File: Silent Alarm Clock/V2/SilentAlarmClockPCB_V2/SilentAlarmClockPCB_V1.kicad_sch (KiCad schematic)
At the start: 28 parts, among them J1 USB_C_Receptacle_USB2.0_16P, J2 Barrel_Jack, J3 B2B-PH-K-S, SW3 RESET, SW4 BOOT, U1 ESD7104MUTAG, U2 ESP32-S3-MINI-1-N8, U3 BQ24040DSQR, U4 TLV75801PDRV

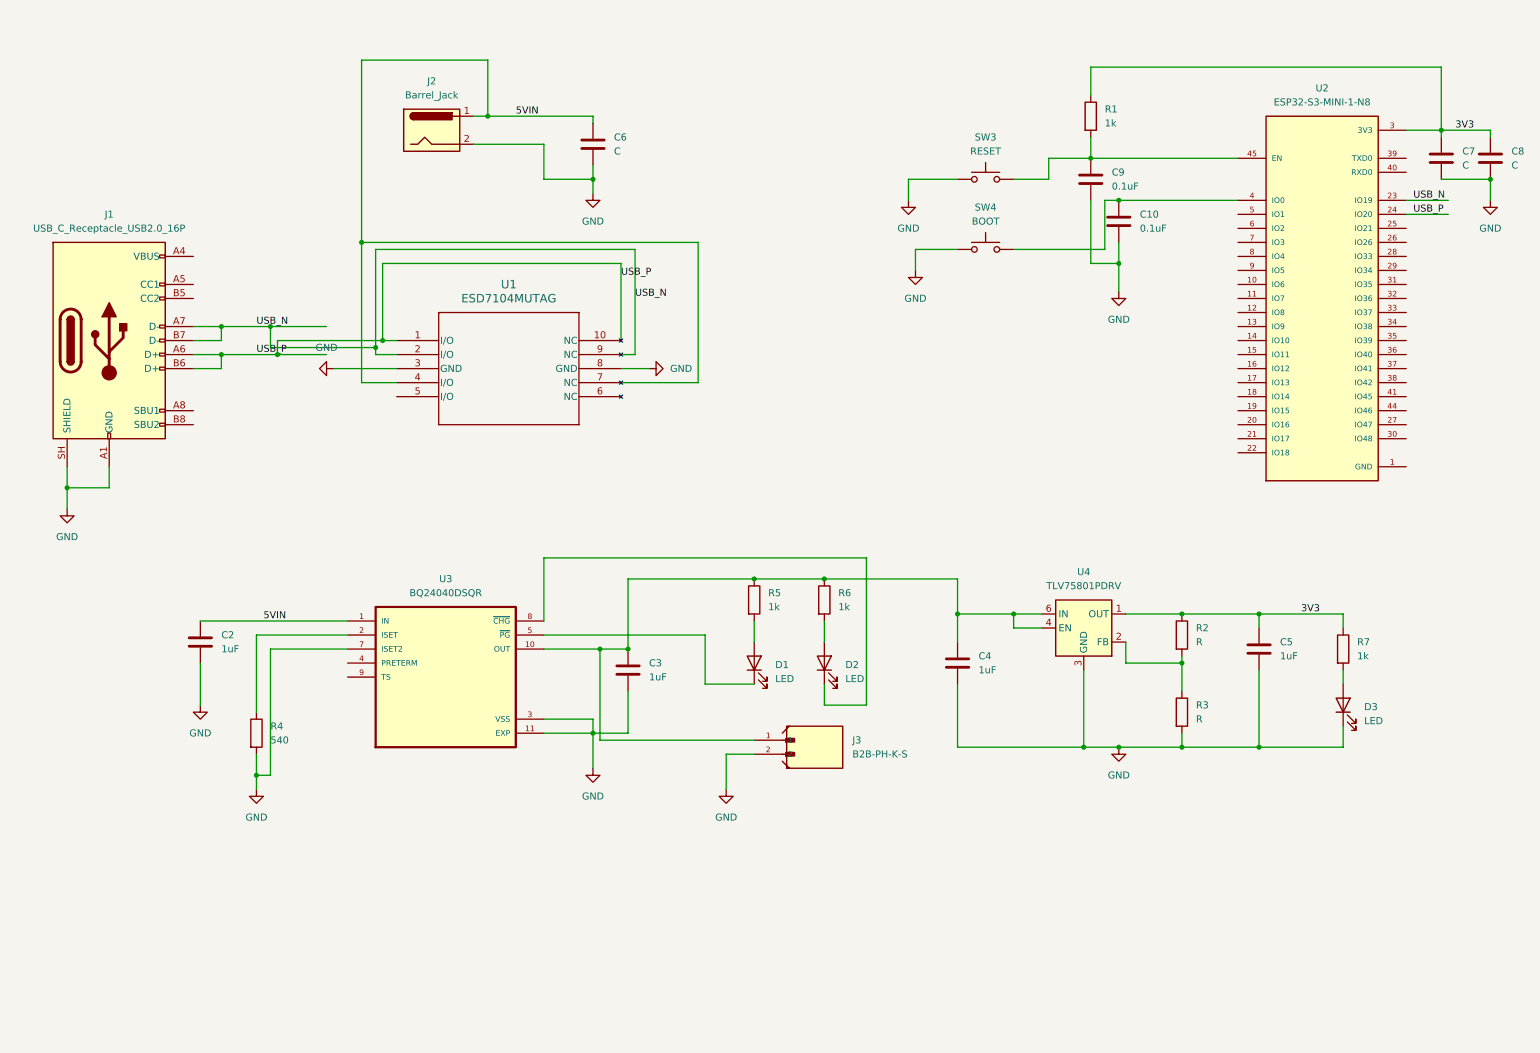
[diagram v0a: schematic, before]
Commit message: Beginning of sparkfun battery babysitter implementation
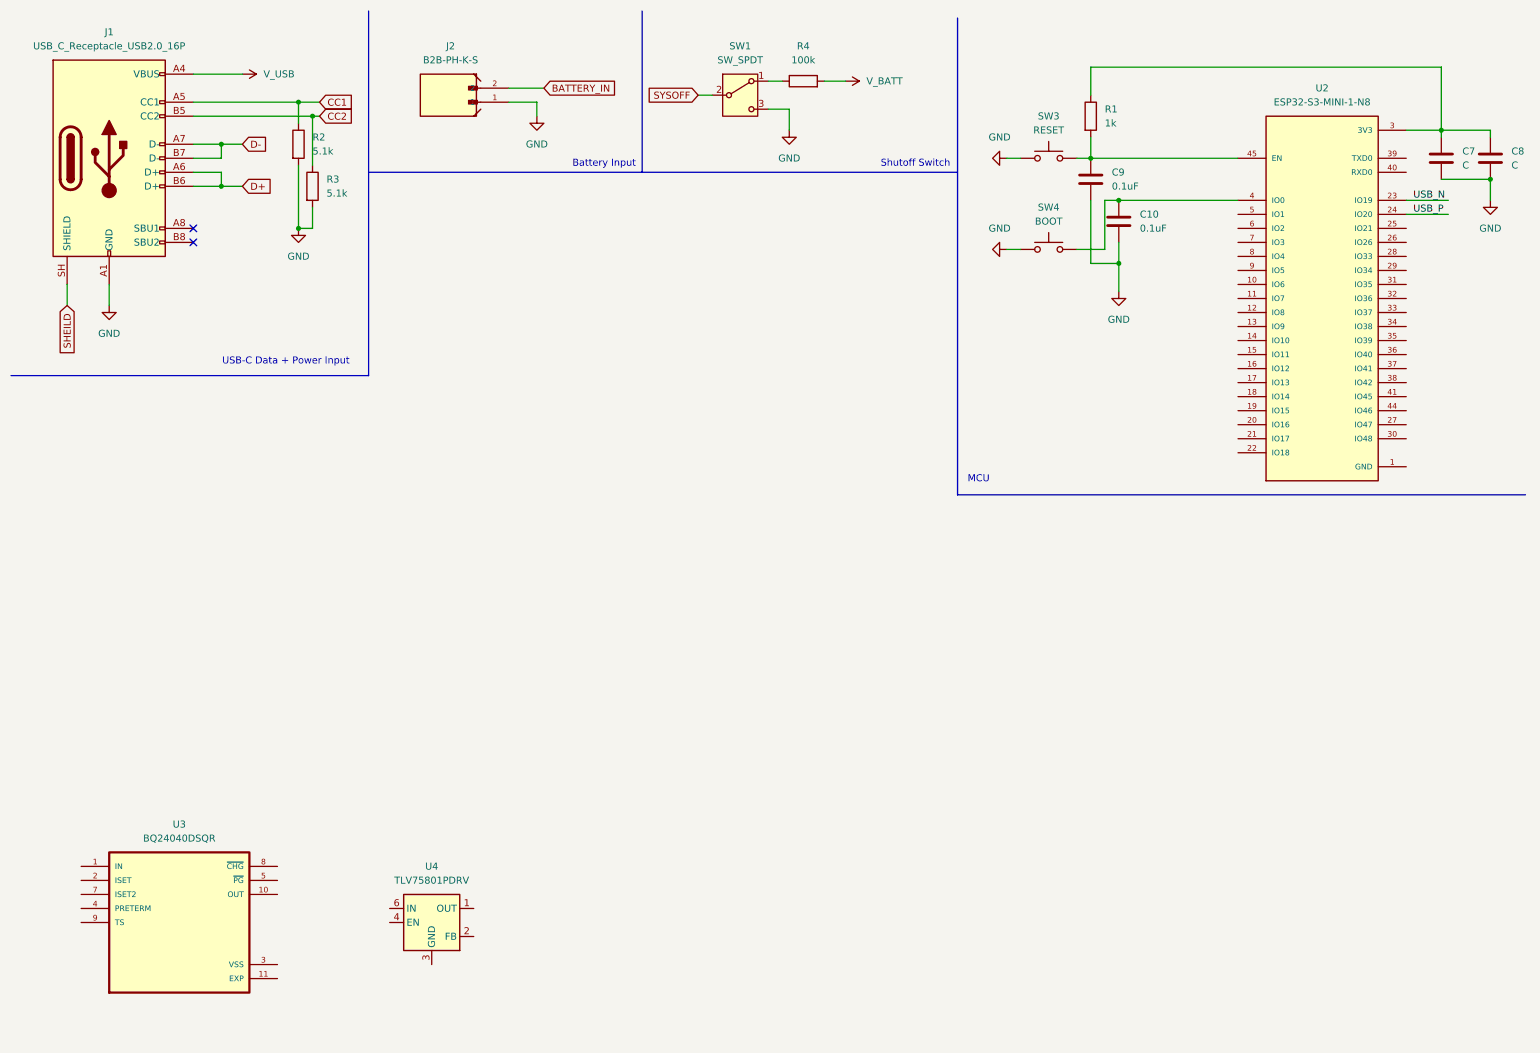
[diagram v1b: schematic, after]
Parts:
- removed C2, C3, C4, C5: 1uF, Capacitor_SMD:C_0603_1608Metric, symbol Device:C
- removed C6: C, Capacitor_SMD:C_0603_1608Metric, symbol Device:C
- removed D1, D2, D3: LED, LED_SMD:LED_0603_1608Metric, symbol Device:LED
- removed J2: Barrel_Jack, Connector_BarrelJack:BarrelJack_CLIFF_FC681465S_SMT_Horizontal, symbol Connector:Barrel_Jack
- removed J3: B2B-PH-K-S, B2B_PH_K_S:JST_B2B-PH-K-S, symbol B2B-PH-K-S:B2B-PH-K-S
- removed R5, R6, R7: 1k, Resistor_SMD:R_0603_1608Metric, symbol Device:R
- removed U1: ESD7104MUTAG, UDFN10_ONS, symbol ESD7104MUTAG:ESD7104MUTAG
- added J2: B2B-PH-K-S, B2B-PH-K-S:JST_B2B-PH-K-S, symbol B2B-PH-K-S:B2B-PH-K-S
- added SW1: SW_SPDT, symbol Switch:SW_SPDT
- R2, R3: value R -> 5.1k
- R4: value 540 -> 100k
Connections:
- net GND: now also R2.2, J2.1, SW1.3 (C); no longer J1.SH (SHIELD), R4.2, U3.11 (EXP), U3.3 (VSS), U3.7 (ISET2), U4.3 (GND), U4.7 (GND)
- net USB_N: no longer J1.A7 (D-), J1.B7 (D-)
- net USB_P: no longer J1.A6 (D+), J1.B6 (D+)
- net at U3.2 (ISET): no longer R4.1
- net V_USB: now reaches J1.A4 (VBUS), J1.A9 (VBUS), J1.B4 (VBUS), J1.B9 (VBUS)
- net CC1: now reaches J1.A5 (CC1)
- net CC1: now also R2.1
- net CC2: now reaches J1.B5 (CC2)
- net CC2: now also R3.1
- net 3V3: no longer names the net of C7.1, C8.1, R1.1, U2.3 (3V3)
- net 3V3: no longer R2.1, U4.1 (OUT)
- net 5VIN: no longer names the net of U3.1 (IN)
- new net: R4.1, SW1.1 (A)
- new net: U4.3 (GND), U4.7 (GND)
- new net BATTERY_IN: J2.2
- new net D+: J1.A6 (D+), J1.B6 (D+)
- new net D-: J1.A7 (D-), J1.B7 (D-)
- new net SHEILD: J1.SH (SHIELD)
- new net SYSOFF: SW1.2 (B)
- new net V_BATT: R4.2
- now unconnected: U3.10 (OUT), U4.2 (FB), U4.4 (EN), U4.6 (IN)
- no-connect marks 0 -> 2
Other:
- note added: "Battery Input"
- note added: "MCU"
- note added: "Shutoff Switch"
- note added: "USB-C Data + Power Input"
- moved on the sheet: J1, SW3, SW4, U3, U4

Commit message: V2 power schematic finished
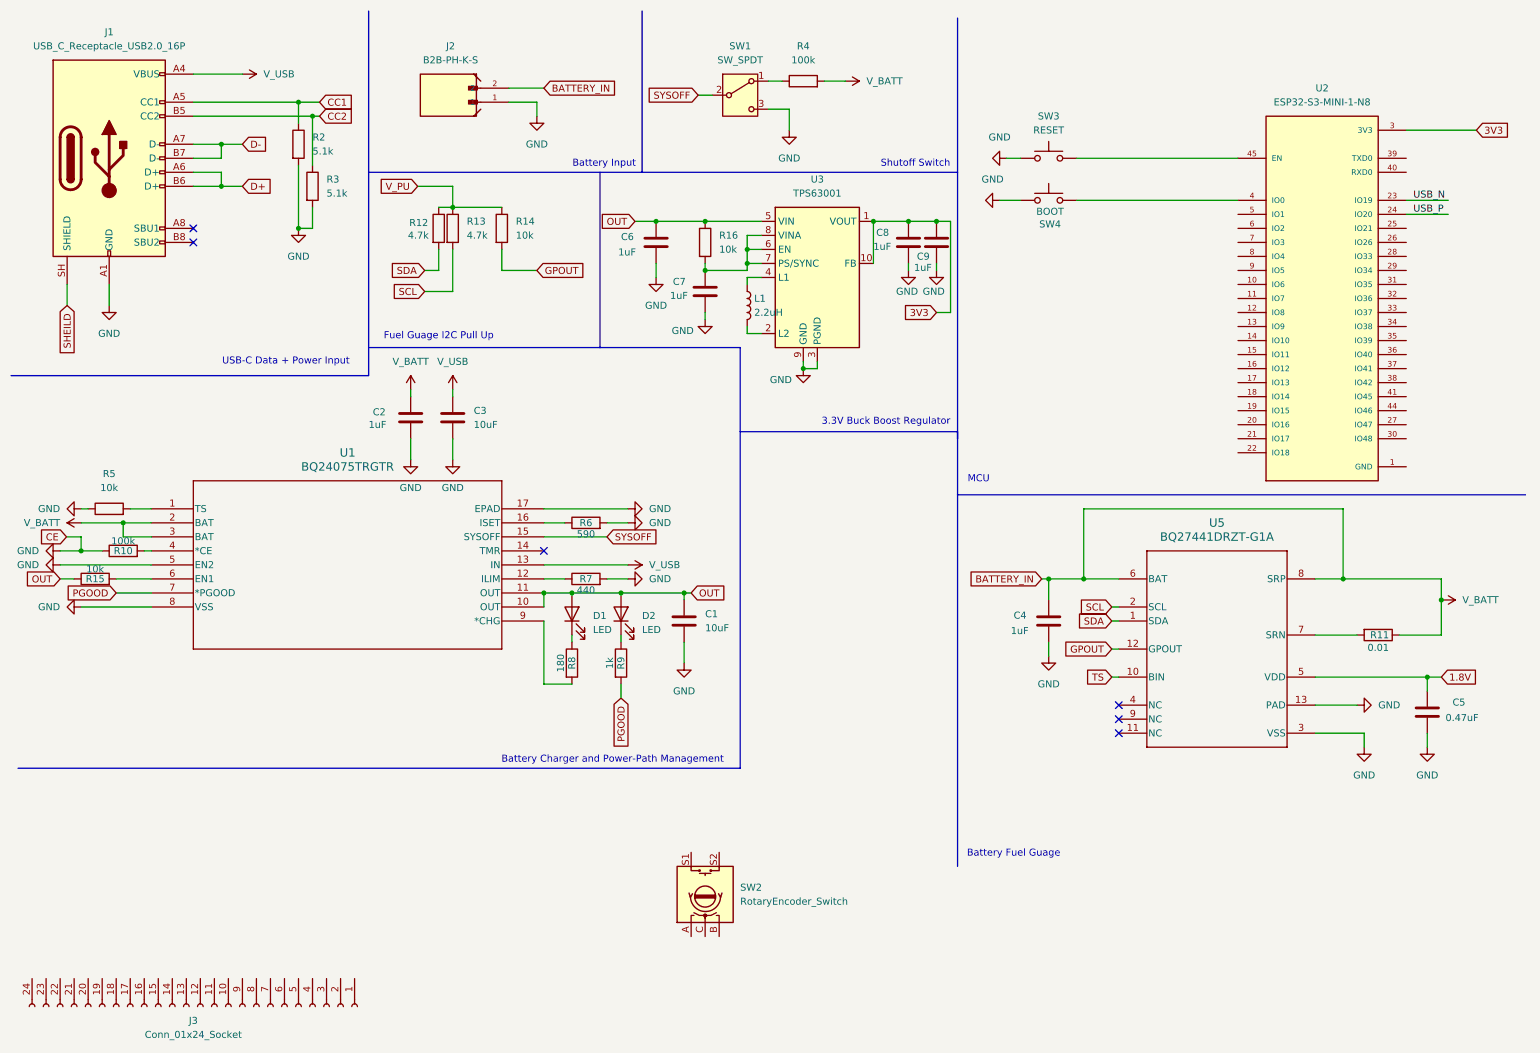
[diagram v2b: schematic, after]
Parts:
- removed C10: 0.1uF, Capacitor_SMD:C_0603_1608Metric, symbol Device:C
- removed R1: 1k, Resistor_SMD:R_0603_1608Metric, symbol Device:R
- removed U3: BQ24040DSQR, BQ24040DSQR:SON40P200X200X80-11N, symbol BQ24040DSQR:BQ24040DSQR
- removed U4: TLV75801PDRV, Package_SON:WSON-6-1EP_2x2mm_P0.65mm_EP1x1.6mm, symbol Regulator_Linear:TLV75801PDRV
- added C1, C3: 10uF, Capacitor_SMD:C_0603_1608Metric, symbol Device:C
- added C2, C4, C6: 1uF, Capacitor_SMD:C_0603_1608Metric, symbol Device:C
- added C5: 0.47uF, Capacitor_SMD:C_0603_1608Metric, symbol Device:C
- added D1, D2: LED, symbol Device:LED
- added J3: Conn_01x24_Socket, Connector_FFC-FPC:Hirose_FH12-24S-0.5SH_1x24-1MP_P0.50mm_Horizontal, symbol Connector:Conn_01x24_Socket
- added L1: 2.2uH, Inductor_SMD:L_1008_2520Metric, symbol Device:L
- added R10: 100k, Resistor_SMD:R_0603_1608Metric, symbol Device:R
- added R11: 0.01, Resistor_SMD:R_0603_1608Metric, symbol Device:R
- added R12, R13: 4.7k, Resistor_SMD:R_0603_1608Metric, symbol Device:R
- added R14, R15, R16, R5: 10k, Resistor_SMD:R_0603_1608Metric, symbol Device:R
- added R6: 590, Resistor_SMD:R_0603_1608Metric, symbol Device:R
- added R7: 440, Resistor_SMD:R_0603_1608Metric, symbol Device:R
- added R8: 180, Resistor_SMD:R_0603_1608Metric, symbol Device:R
- added R9: 1k, Resistor_SMD:R_0603_1608Metric, symbol Device:R
- added SW2: RotaryEncoder_Switch, symbol Device:RotaryEncoder_Switch
- added U1: BQ24075TRGTR, RGT16_1P7X1P7, symbol 2026-08-07_15-47-46:BQ24075TRGTR
- added U3: TPS63001, Package_SON:Texas_DRC0010J_ThermalVias, symbol Regulator_Switching:TPS63001
- added U5: BQ27441DRZT-G1A, Copy of DRZ0012A, symbol BQ27441-G1A:BQ27441DRZT-G1A
- C7, C8: value C -> 1uF
- C9: value 0.1uF -> 1uF
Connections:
- net BATTERY_IN is gone; now on net V_BATT: J2.2
- net GND: now also C7.1, C8.1, C9.1, C1.2, C2.2, C3.2, C4.1, C5.1, C6.1, R10.1, R5.1, R6.2, R7.2, U1.17 (EPAD), U1.5 (EN2), U1.8 (VSS), U3.11 (PGND), U3.3 (PGND), U3.9 (GND), U5.13 (PAD), U5.3 (VSS); no longer C7.2, C8.2, C9.2
- net SYSOFF: now also U1.15 (SYSOFF)
- net V_BATT: now also C2.1, C4.2, R11.1, U1.2 (BAT), U1.3 (BAT), U5.6 (BAT), U5.8 (SRP)
- net V_USB: now also C3.1, U1.13 (IN)
- net at SW3.2, U2.45 (EN): no longer C9.1
- new net: R11.2, U5.7 (SRN)
- new net: D1.1 (K), R8.1
- new net: R8.2, U1.9 (*CHG)
- new net: R5.2, U1.1 (TS)
- new net: D2.1 (K), R9.1
- new net: L1.1, U3.4 (L1)
- new net: L1.2, U3.2 (L2)
- new net: C7.2, R16.2, U3.6 (EN), U3.7 (PS/SYNC), U3.8 (VINA)
- new net: R10.2, U1.4 (*CE)
- new net: R15.2, U1.6 (EN1)
- new net: R7.1, U1.12 (ILIM)
- new net: R6.1, U1.16 (ISET)
- new net 1.8V: C5.2, U5.5 (VDD)
- new net 3V3: C8.2, C9.2, U2.3 (3V3), U3.1 (VOUT), U3.10 (FB)
- new net GPOUT: R14.2, U5.12 (GPOUT)
- new net OUT: C1.1, C6.2, D1.2 (A), D2.2 (A), R15.1, R16.1, U1.10 (OUT), U1.11 (OUT), U3.5 (VIN)
- new net PGOOD: R9.2, U1.7 (*PGOOD)
- new net SCL: R13.2, U5.2 (SCL)
- new net SDA: R12.2, U5.1 (SDA)
- new net TS: U5.10 (BIN)
- new net V_PU: R12.1, R13.1, R14.1
- no-connect marks 2 -> 6
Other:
- note added: "3.3V Buck Boost Regulator"
- note added: "Battery Charger and Power-Path Management"
- note added: "Battery Fuel Guage"
- note added: "Fuel Guage I2C Pull Up"
- moved on the sheet: SW4

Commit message: V2 preliminary schematic finished
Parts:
- removed J3: Conn_01x24_Socket, Connector_FFC-FPC:Hirose_FH12-24S-0.5SH_1x24-1MP_P0.50mm_Horizontal, symbol Connector:Conn_01x24_Socket
- added C10, C11: 1uF, Capacitor_SMD:C_0603_1608Metric, symbol Device:C
- added C12, C13: 0.1uF, Capacitor_SMD:C_0603_1608Metric, symbol Device:C
- added J3: Conn_01x08_Socket, Connector_JST:JST_PH_B8B-PH-K_1x08_P2.00mm_Vertical, symbol Connector:Conn_01x08_Socket
- added R17, R18, R19: 10k, Resistor_SMD:R_0603_1608Metric, symbol Device:R
- added U4: ESD7104MUTAG, UDFN10_ONS, symbol ESD7104MUTAG:ESD7104MUTAG
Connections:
- net USB_N is gone; now on net D-: U2.23 (IO19)
- net USB_P is gone; now on net D+: U2.24 (IO20)
- net V_PU is gone; now on net 3V3: R12.1, R13.1, R14.1
- net 3V3: now also J3.1 (Pin_1), R19.1
- net D+: now also U4.2 (I/O), U4.9 (NC)
- net D-: now also U4.1 (I/O), U4.10 (NC)
- net GND: now also SW2.C, SW2.S2, C10.1, C11.1, J3.2 (Pin_2), U4.3 (GND), U4.8 (GND)
- net SCL: now also U2.13 (IO9)
- net SDA: now also U2.12 (IO8)
- net V_USB: now also U4.4 (I/O), U4.7 (NC)
- net at SW2.A: now also R17.2
- net at SW2.B: now also R18.1
- net S1: now reaches SW2.S1
- net S1: now also U2.25 (IO21)
- net at SW4.2, U2.4 (IO0): now also C13.2
- net at SW3.2, U2.45 (EN): now also C12.2, R19.2
- net CS: now reaches U2.14 (IO10)
- net CS: now also J3.5 (Pin_5)
- net DIN: now reaches U2.15 (IO11)
- net DIN: now also J3.3 (Pin_3)
- net CLK: now reaches U2.16 (IO12)
- net CLK: now also J3.4 (Pin_4)
- net D/C: now reaches U2.17 (IO13)
- net D/C: now also J3.6 (Pin_6)
- net RST: now reaches U2.18 (IO14)
- net RST: now also J3.7 (Pin_7)
- net BUSY: now reaches U2.19 (IO15)
- net BUSY: now also J3.8 (Pin_8)
- net Encoder_A: now reaches U2.28 (IO33)
- net Encoder_A: now also C10.2, R17.1
- net Encoder_B: now reaches U2.29 (IO34)
- net Encoder_B: now also C11.2, R18.2
- new net: C12.1, C13.1
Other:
- note added: "Display Connector"
- note added: "ESD Protection"
- note added: "Encoder + Button"
- moved on the sheet: SW2, SW4

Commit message: V2 preliminary layout
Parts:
- D1: footprint (none) -> LED_SMD:LED_0603_1608Metric_Pad1.05x0.95mm_HandSolder
- D2: footprint (none) -> LED_SMD:LED_0603_1608Metric
- SW1: footprint (none) -> Button_Switch_SMD:SW_SPDT_CK_JS102011SAQN
- SW2: footprint (none) -> PEC11R_4220F_S0024:XDCR_PEC11R-4220F-S0024
- U1: footprint RGT16_1P7X1P7 -> BQ24075TRGTR:RGT16_1P7X1P7
- U4: footprint UDFN10_ONS -> ESD7104MUTAG:UDFN10_ONS
- U5: footprint Copy of DRZ0012A -> BQ27441DRZT-G1A:Copy of DRZ0012A
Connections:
- no-connect marks 6 -> 34
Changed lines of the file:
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@@
 	)
 	(no_connect
+		(at 264.16 83.82)
+	)
+	(no_connect
+		(at 124.46 180.34)
+	)
+	(no_connect
+		(at 264.16 68.58)
+	)
+	(no_connect
+		(at 233.68 86.36)
+	)
+	(no_connect
+		(at 264.16 64.77)
+	)
+	(no_connect
 		(at 107.95 109.22)
 	)
 	(no_connect
+		(at 264.16 40.64)
+	)
+	(no_connect
+		(at 233.68 60.96)
+	)
+	(no_connect
+		(at 233.68 63.5)
+	)
+	(no_connect
+		(at 264.16 81.28)
+	)
+	(no_connect
+		(at 264.16 88.9)
+	)
+	(no_connect
+		(at 233.68 55.88)
+	)
+	(no_connect
+		(at 264.16 53.34)
+	)
+	(no_connect
+		(at 264.16 73.66)
+	)
+	(no_connect
+		(at 264.16 78.74)
+	)
+	(no_connect
 		(at 212.09 139.7)
 	)
 	(no_connect
+		(at 264.16 66.04)
+	)
+	(no_connect
+		(at 233.68 48.26)
+	)
+	(no_connect
 		(at 212.09 142.24)
 	)
 	(no_connect
+		(at 233.68 58.42)
+	)
+	(no_connect
+		(at 264.16 60.96)
+	)
+	(no_connect
+		(at 233.68 53.34)
+	)
+	(no_connect
 		(at 44.45 53.34)
 	)
 	(no_connect
+		(at 233.68 88.9)
+	)
+	(no_connect
+		(at 264.16 38.1)
+	)
+	(no_connect
+		(at 233.68 91.44)
+	)
+	(no_connect
+		(at 165.1 180.34)
+	)
+	(no_connect
+		(at 264.16 71.12)
+	)
+	(no_connect
+		(at 233.68 50.8)
+	)
+	(no_connect
+		(at 264.16 86.36)
+	)
+	(no_connect
+		(at 264.16 76.2)
+	)
+	(no_connect
+		(at 264.16 63.5)
+	)
+	(no_connect
 		(at 212.09 137.16)
 	)
@@
 	(wire
 		(pts
+			(xy 264.16 93.98) (xy 269.24 93.98)
+		)
+		(stroke
+			(width 0)
+			(type default)
+		)
+	)
+	(wire
+		(pts
 			(xy 86.36 187.96) (xy 86.36 191.77)
 		)
@@
 			)
 		)
-		(property "Footprint" ""
+		(property "Footprint" "PEC11R_4220F_S0024:XDCR_PEC11R-4220F-S0024"
 			(at 68.326 171.45 0)
 			(hide yes)
@@
 			)
 		)
-		(property "Footprint" "Copy of DRZ0012A"
+		(property "Footprint" "BQ27441DRZT-G1A:Copy of DRZ0012A"
 			(at 229.87 127 0)
 			(hide yes)
@@
 			)
 		)
-		(property "Footprint" ""
+		(property "Footprint" "LED_SMD:LED_0603_1608Metric"
 			(at 121.92 120.65 0)
 			(hide yes)
@@
 			)
 		)
-		(property "Footprint" ""
+		(property "Footprint" "LED_SMD:LED_0603_1608Metric_Pad1.05x0.95mm_HandSolder"
 			(at 113.03 120.65 0)
 			(hide yes)
@@
 			)
 		)
-		(property "Footprint" "UDFN10_ONS"
+		(property "Footprint" "ESD7104MUTAG:UDFN10_ONS"
 			(at 124.46 170.18 0)
 			(hide yes)
@@
 			)
 		)
-		(property "Footprint" ""
+		(property "Footprint" "Button_Switch_SMD:SW_SPDT_CK_JS102011SAQN"
 			(at 143.51 26.67 0)
 			(hide yes)
@@
 			)
 		)
-		(property "Footprint" "RGT16_1P7X1P7"
+		(property "Footprint" "BQ24075TRGTR:RGT16_1P7X1P7"
 			(at 36.83 101.6 0)
 			(hide yes)
@@
 					(unit 1)
 				)
+			)
+		)
+	)
+	(symbol
+		(lib_id "power:GND")
+		(at 269.24 93.98 90)
+		(unit 1)
+		(body_style 1)
+		(exclude_from_sim no)
+		(in_bom yes)
+		(on_board yes)
+		(in_pos_files yes)
+		(dnp no)
+		(fields_autoplaced yes)
+		(property "Reference" "#PWR041"
+			(at 275.59 93.98 0)
+			(hide yes)
+			(show_name no)
+			(do_not_autoplace no)
+			(effects
+				(font
+					(size 1.27 1.27)
+				)
+			)
+		)
+		(property "Value" "GND"
+			(at 273.05 93.9799 90)
+			(show_name no)
+			(do_not_autoplace no)
+			(effects
+				(font
+					(size 1.27 1.27)
+				)
+				(justify right)
+			)
+		)
+		(property "Footprint" ""
+			(at 269.24 93.98 0)
+			(hide yes)
+			(show_name no)
+			(do_not_autoplace no)
+			(effects
+				(font
+					(size 1.27 1.27)
+				)
+			)
+		)
+		(property "Datasheet" ""
+			(at 269.24 93.98 0)
+			(hide yes)
+			(show_name no)
+			(do_not_autoplace no)
+			(effects
+				(font
+					(size 1.27 1.27)
+				)
+			)
+		)
+		(property "Description" "Power symbol creates a global label with name \"GND\" , ground"
+			(at 269.24 93.98 0)
+			(hide yes)
+			(show_name no)
+			(do_not_autoplace no)
+			(effects
+				(font
+					(size 1.27 1.27)
+				)
+			)
+		)
+		(pin "1"
+		)
+		(instances
+			(project "SilentAlarmClockPCB_V1"
+				(path "/9e0581d1-a9e9-4515-9473-537630af280a"
+					(reference "#PWR041")
+					(unit 1)
+				)

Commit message: V2 most non pwr traces added
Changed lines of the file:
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@@
 		(in_pos_files yes)
 		(dnp no)
-		(fields_autoplaced yes)
 		(property "Reference" "#PWR038"
 			(at 123.19 179.07 0)
@@
 		)
 		(property "Value" "V_USB"
-			(at 115.57 179.0699 90)
+			(at 118.364 181.864 90)
 			(show_name no)
 			(do_not_autoplace no)
